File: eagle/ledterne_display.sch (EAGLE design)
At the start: 5 parts

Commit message: - Added possible routing (one layer only).
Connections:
- new net N$4: JP1.1, R1.2
- new net N$5: JP1.2, R2.2
- new net N$6: JP1.3, R3.2
- net GND: now also JP1.4
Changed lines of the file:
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@@
 <sheet>
 <plain>
-<text x="15.24" y="96.52" size="1.778" layer="97">TODO: name pins (GND, R, G, B)</text>
+<text x="35.56" y="96.52" size="1.778" layer="97">TODO: name pins (GND, R, G, B)</text>
 </plain>
 <instances>
@@
 <net name="GND" class="0">
 <segment>
+<pinref part="LED1" gate="G$1" pin="CBLUE"/>
+<wire x1="25.4" y1="53.34" x2="25.4" y2="40.64" width="0.1524" layer="91"/>
+<pinref part="GND3" gate="1" pin="GND"/>
+<pinref part="JP1" gate="A" pin="4"/>
+<wire x1="7.62" y1="99.06" x2="33.02" y2="99.06" width="0.1524" layer="91"/>
+<wire x1="33.02" y1="99.06" x2="33.02" y2="40.64" width="0.1524" layer="91"/>
+<wire x1="33.02" y1="40.64" x2="25.4" y2="40.64" width="0.1524" layer="91"/>
+<junction x="25.4" y="40.64"/>
 <pinref part="GND1" gate="1" pin="GND"/>
 <pinref part="LED1" gate="G$1" pin="CGREEN"/>
 <wire x1="20.32" y1="53.34" x2="20.32" y2="40.64" width="0.1524" layer="91"/>
-</segment>
-<segment>
+<wire x1="25.4" y1="40.64" x2="20.32" y2="40.64" width="0.1524" layer="91"/>
+<junction x="20.32" y="40.64"/>
 <pinref part="LED1" gate="G$1" pin="CRED"/>
 <wire x1="15.24" y1="53.34" x2="15.24" y2="40.64" width="0.1524" layer="91"/>
 <pinref part="GND2" gate="1" pin="GND"/>
-</segment>
-<segment>
-<pinref part="LED1" gate="G$1" pin="CBLUE"/>
-<wire x1="25.4" y1="53.34" x2="25.4" y2="40.64" width="0.1524" layer="91"/>
-<pinref part="GND3" gate="1" pin="GND"/>
+<wire x1="20.32" y1="40.64" x2="15.24" y2="40.64" width="0.1524" layer="91"/>
+<junction x="15.24" y="40.64"/>
 </segment>
 </net>
+<net name="N$4" class="0">
+<segment>
+<pinref part="JP1" gate="A" pin="1"/>
+<pinref part="R1" gate="G$1" pin="2"/>
+<wire x1="7.62" y1="91.44" x2="15.24" y2="91.44" width="0.1524" layer="91"/>
+<wire x1="15.24" y1="91.44" x2="15.24" y2="81.28" width="0.1524" layer="91"/>
+</segment>
+</net>
+<net name="N$5" class="0">
+<segment>
+<pinref part="JP1" gate="A" pin="2"/>
+<pinref part="R2" gate="G$1" pin="2"/>
+<wire x1="7.62" y1="93.98" x2="20.32" y2="93.98" width="0.1524" layer="91"/>
+<wire x1="20.32" y1="93.98" x2="20.32" y2="81.28" width="0.1524" layer="91"/>
+</segment>
+</net>
+<net name="N$6" class="0">
+<segment>
+<pinref part="JP1" gate="A" pin="3"/>
+<pinref part="R3" gate="G$1" pin="2"/>
+<wire x1="7.62" y1="96.52" x2="25.4" y2="96.52" width="0.1524" layer="91"/>
+<wire x1="25.4" y1="96.52" x2="25.4" y2="81.28" width="0.1524" layer="91"/>
+</segment>
+</net>

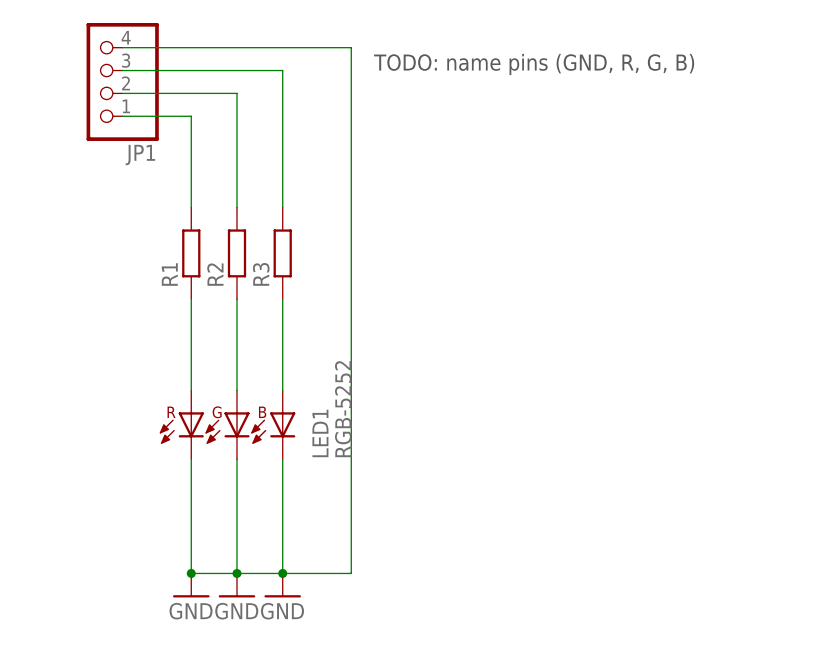
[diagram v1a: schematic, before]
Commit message: Clean up the schematic a little bit
Making everything a bit more compact and using less wires.
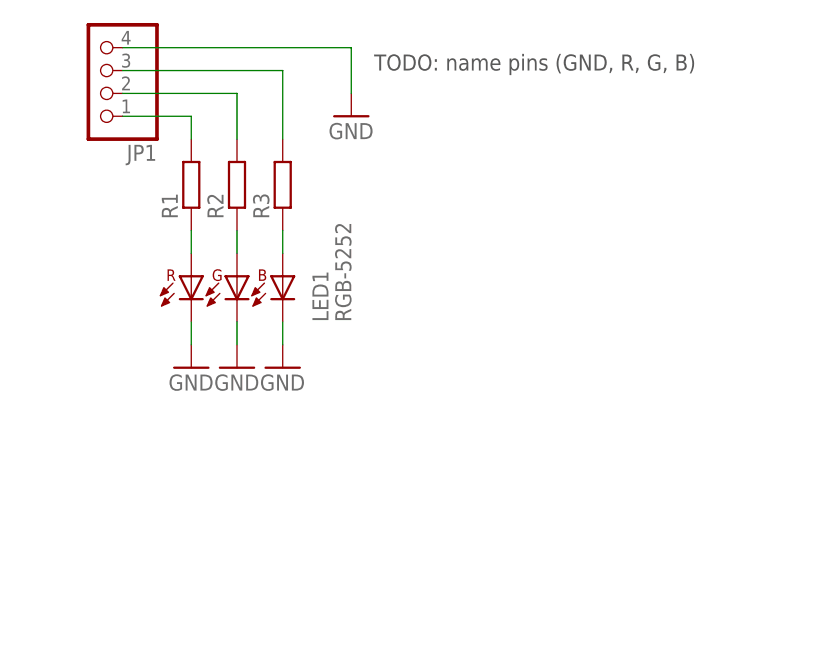
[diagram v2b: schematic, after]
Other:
- moved on the sheet: LED1, R1, R2, R3
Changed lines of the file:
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@@
 <part name="GND3" library="supply1" deviceset="GND" device=""/>
 <part name="JP1" library="pinhead" deviceset="PINHD-1X4" device=""/>
+<part name="GND4" library="supply1" deviceset="GND" device=""/>
 </parts>
 <sheets>
@@
 </plain>
 <instances>
-<instance part="LED1" gate="G$1" x="20.32" y="55.88"/>
-<instance part="R1" gate="G$1" x="15.24" y="76.2" rot="R90"/>
-<instance part="R2" gate="G$1" x="20.32" y="76.2" rot="R90"/>
-<instance part="R3" gate="G$1" x="25.4" y="76.2" rot="R90"/>
-<instance part="GND1" gate="1" x="20.32" y="38.1"/>
-<instance part="GND2" gate="1" x="15.24" y="38.1"/>
-<instance part="GND3" gate="1" x="25.4" y="38.1"/>
+<instance part="LED1" gate="G$1" x="20.32" y="71.12"/>
+<instance part="R1" gate="G$1" x="15.24" y="83.82" rot="R90"/>
+<instance part="R2" gate="G$1" x="20.32" y="83.82" rot="R90"/>
+<instance part="R3" gate="G$1" x="25.4" y="83.82" rot="R90"/>
+<instance part="GND1" gate="1" x="20.32" y="63.5"/>
+<instance part="GND2" gate="1" x="15.24" y="63.5"/>
+<instance part="GND3" gate="1" x="25.4" y="63.5"/>
 <instance part="JP1" gate="A" x="5.08" y="96.52" rot="R180"/>
+<instance part="GND4" gate="1" x="33.02" y="91.44"/>
 </instances>
 <busses>
@@
 <pinref part="R1" gate="G$1" pin="1"/>
 <pinref part="LED1" gate="G$1" pin="ARED"/>
-<wire x1="15.24" y1="71.12" x2="15.24" y2="60.96" width="0.1524" layer="91"/>
+<wire x1="15.24" y1="78.74" x2="15.24" y2="76.2" width="0.1524" layer="91"/>
 </segment>
 </net>
@@
 <pinref part="R2" gate="G$1" pin="1"/>
 <pinref part="LED1" gate="G$1" pin="AGREEN"/>
-<wire x1="20.32" y1="71.12" x2="20.32" y2="60.96" width="0.1524" layer="91"/>
+<wire x1="20.32" y1="78.74" x2="20.32" y2="76.2" width="0.1524" layer="91"/>
 </segment>
 </net>
@@
 <pinref part="R3" gate="G$1" pin="1"/>
 <pinref part="LED1" gate="G$1" pin="ABLUE"/>
-<wire x1="25.4" y1="71.12" x2="25.4" y2="60.96" width="0.1524" layer="91"/>
+<wire x1="25.4" y1="78.74" x2="25.4" y2="76.2" width="0.1524" layer="91"/>
 </segment>
 </net>
 <net name="GND" class="0">
 <segment>
+<pinref part="LED1" gate="G$1" pin="CRED"/>
+<wire x1="15.24" y1="68.58" x2="15.24" y2="66.04" width="0.1524" layer="91"/>
+<pinref part="GND2" gate="1" pin="GND"/>
+</segment>
+<segment>
+<pinref part="GND1" gate="1" pin="GND"/>
+<pinref part="LED1" gate="G$1" pin="CGREEN"/>
+<wire x1="20.32" y1="68.58" x2="20.32" y2="66.04" width="0.1524" layer="91"/>
+</segment>
+<segment>
 <pinref part="LED1" gate="G$1" pin="CBLUE"/>
-<wire x1="25.4" y1="53.34" x2="25.4" y2="40.64" width="0.1524" layer="91"/>
+<wire x1="25.4" y1="68.58" x2="25.4" y2="66.04" width="0.1524" layer="91"/>
 <pinref part="GND3" gate="1" pin="GND"/>
+</segment>
+<segment>
 <pinref part="JP1" gate="A" pin="4"/>
 <wire x1="7.62" y1="99.06" x2="33.02" y2="99.06" width="0.1524" layer="91"/>
-<wire x1="33.02" y1="99.06" x2="33.02" y2="40.64" width="0.1524" layer="91"/>
-<wire x1="33.02" y1="40.64" x2="25.4" y2="40.64" width="0.1524" layer="91"/>
-<junction x="25.4" y="40.64"/>
-<pinref part="GND1" gate="1" pin="GND"/>
-<pinref part="LED1" gate="G$1" pin="CGREEN"/>
-<wire x1="20.32" y1="53.34" x2="20.32" y2="40.64" width="0.1524" layer="91"/>
-<wire x1="25.4" y1="40.64" x2="20.32" y2="40.64" width="0.1524" layer="91"/>
-<junction x="20.32" y="40.64"/>
-<pinref part="LED1" gate="G$1" pin="CRED"/>
-<wire x1="15.24" y1="53.34" x2="15.24" y2="40.64" width="0.1524" layer="91"/>
-<pinref part="GND2" gate="1" pin="GND"/>
-<wire x1="20.32" y1="40.64" x2="15.24" y2="40.64" width="0.1524" layer="91"/>
-<junction x="15.24" y="40.64"/>
+<wire x1="33.02" y1="99.06" x2="33.02" y2="93.98" width="0.1524" layer="91"/>
+<pinref part="GND4" gate="1" pin="GND"/>
 </segment>
 </net>
@@
 <pinref part="R1" gate="G$1" pin="2"/>
 <wire x1="7.62" y1="91.44" x2="15.24" y2="91.44" width="0.1524" layer="91"/>
-<wire x1="15.24" y1="91.44" x2="15.24" y2="81.28" width="0.1524" layer="91"/>
+<wire x1="15.24" y1="91.44" x2="15.24" y2="88.9" width="0.1524" layer="91"/>
 </segment>
 </net>
@@
 <pinref part="R2" gate="G$1" pin="2"/>
 <wire x1="7.62" y1="93.98" x2="20.32" y2="93.98" width="0.1524" layer="91"/>
-<wire x1="20.32" y1="93.98" x2="20.32" y2="81.28" width="0.1524" layer="91"/>
+<wire x1="20.32" y1="93.98" x2="20.32" y2="88.9" width="0.1524" layer="91"/>
 </segment>
 </net>
@@
 <pinref part="R3" gate="G$1" pin="2"/>
 <wire x1="7.62" y1="96.52" x2="25.4" y2="96.52" width="0.1524" layer="91"/>
-<wire x1="25.4" y1="96.52" x2="25.4" y2="81.28" width="0.1524" layer="91"/>
+<wire x1="25.4" y1="96.52" x2="25.4" y2="88.9" width="0.1524" layer="91"/>
 </segment>
 </net>

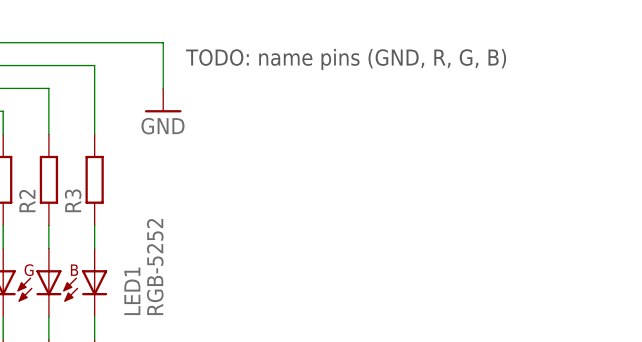
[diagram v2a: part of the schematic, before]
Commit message: Assign net names to the LED inputs
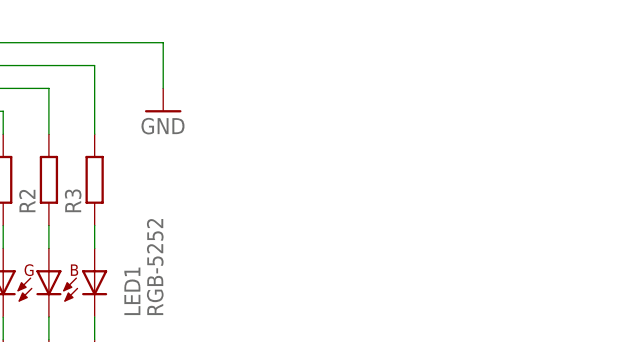
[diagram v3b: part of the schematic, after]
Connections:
- net N$4 renamed LED_R
- net N$5 renamed LED_G
- net N$6 renamed LED_B
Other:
- note removed: "TODO: name pins (GND, R, G, B)"
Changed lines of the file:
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@@
 <sheet>
 <plain>
-<text x="35.56" y="96.52" size="1.778" layer="97">TODO: name pins (GND, R, G, B)</text>
 </plain>
 <instances>
@@
 </segment>
 </net>
-<net name="N$4" class="0">
+<net name="LED_R" class="0">
 <segment>
 <pinref part="JP1" gate="A" pin="1"/>
@@
 </segment>
 </net>
-<net name="N$5" class="0">
+<net name="LED_G" class="0">
 <segment>
 <pinref part="JP1" gate="A" pin="2"/>
@@
 </segment>
 </net>
-<net name="N$6" class="0">
+<net name="LED_B" class="0">
 <segment>
 <pinref part="JP1" gate="A" pin="3"/>

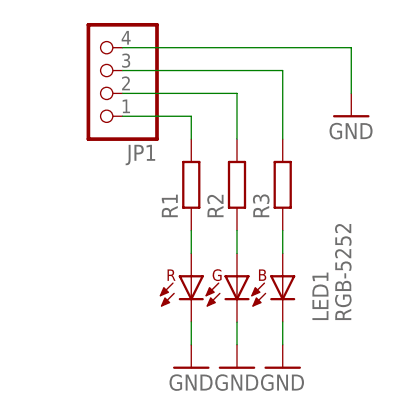
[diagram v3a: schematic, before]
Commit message: Update routing to be more compact
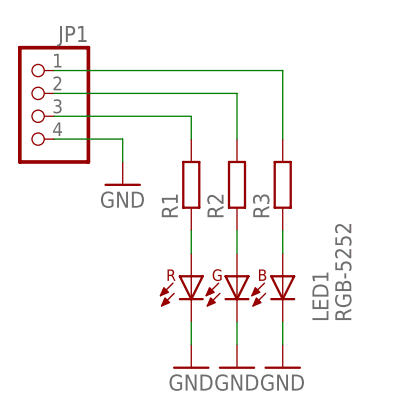
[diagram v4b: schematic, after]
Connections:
- net LED_B: now also JP1.1; no longer JP1.3
- net LED_R: now also JP1.3; no longer JP1.1
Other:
- moved on the sheet: JP1
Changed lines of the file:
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@@
 <instance part="GND2" gate="1" x="15.24" y="63.5"/>
 <instance part="GND3" gate="1" x="25.4" y="63.5"/>
-<instance part="JP1" gate="A" x="5.08" y="96.52" rot="R180"/>
-<instance part="GND4" gate="1" x="33.02" y="91.44"/>
+<instance part="JP1" gate="A" x="-2.54" y="91.44" rot="MR0"/>
+<instance part="GND4" gate="1" x="7.62" y="83.82"/>
 </instances>
 <busses>
@@
 <segment>
 <pinref part="JP1" gate="A" pin="4"/>
-<wire x1="7.62" y1="99.06" x2="33.02" y2="99.06" width="0.1524" layer="91"/>
-<wire x1="33.02" y1="99.06" x2="33.02" y2="93.98" width="0.1524" layer="91"/>
+<wire x1="0" y1="88.9" x2="7.62" y2="88.9" width="0.1524" layer="91"/>
+<wire x1="7.62" y1="88.9" x2="7.62" y2="86.36" width="0.1524" layer="91"/>
 <pinref part="GND4" gate="1" pin="GND"/>
 </segment>
@@
 <net name="LED_R" class="0">
 <segment>
-<pinref part="JP1" gate="A" pin="1"/>
 <pinref part="R1" gate="G$1" pin="2"/>
-<wire x1="7.62" y1="91.44" x2="15.24" y2="91.44" width="0.1524" layer="91"/>
 <wire x1="15.24" y1="91.44" x2="15.24" y2="88.9" width="0.1524" layer="91"/>
+<pinref part="JP1" gate="A" pin="3"/>
+<wire x1="0" y1="91.44" x2="15.24" y2="91.44" width="0.1524" layer="91"/>
 </segment>
 </net>
@@
 <pinref part="JP1" gate="A" pin="2"/>
 <pinref part="R2" gate="G$1" pin="2"/>
-<wire x1="7.62" y1="93.98" x2="20.32" y2="93.98" width="0.1524" layer="91"/>
+<wire x1="0" y1="93.98" x2="20.32" y2="93.98" width="0.1524" layer="91"/>
 <wire x1="20.32" y1="93.98" x2="20.32" y2="88.9" width="0.1524" layer="91"/>
 </segment>
@@
 <net name="LED_B" class="0">
 <segment>
-<pinref part="JP1" gate="A" pin="3"/>
 <pinref part="R3" gate="G$1" pin="2"/>
-<wire x1="7.62" y1="96.52" x2="25.4" y2="96.52" width="0.1524" layer="91"/>
 <wire x1="25.4" y1="96.52" x2="25.4" y2="88.9" width="0.1524" layer="91"/>
+<pinref part="JP1" gate="A" pin="1"/>
+<wire x1="0" y1="96.52" x2="25.4" y2="96.52" width="0.1524" layer="91"/>
 </segment>
 </net>
